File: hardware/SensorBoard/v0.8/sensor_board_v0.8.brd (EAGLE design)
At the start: 52.5 x 43 mm, 48 parts, among them IC1 BMP280, J3 USB-MICROB, U10 CCS811, U11 RFM69HW, U2 TSL2561, U3 ATMEGA328P-MU, U7 SHT31, U8 MCP1703/3.3V, U9 MCP1703CB, Y1 16MHZ

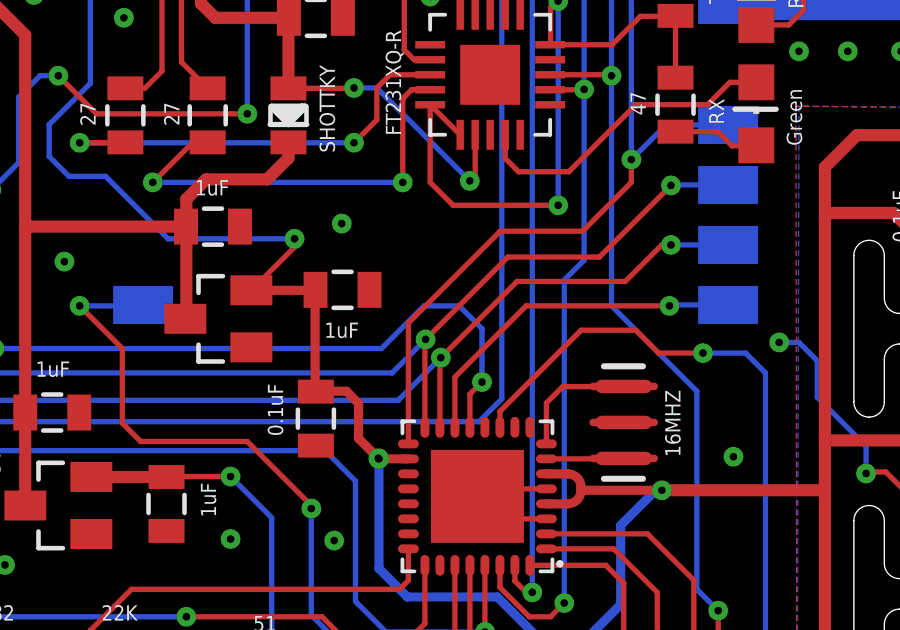
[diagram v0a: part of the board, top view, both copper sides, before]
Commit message: Adjusted distance between MISO and MOSI vias
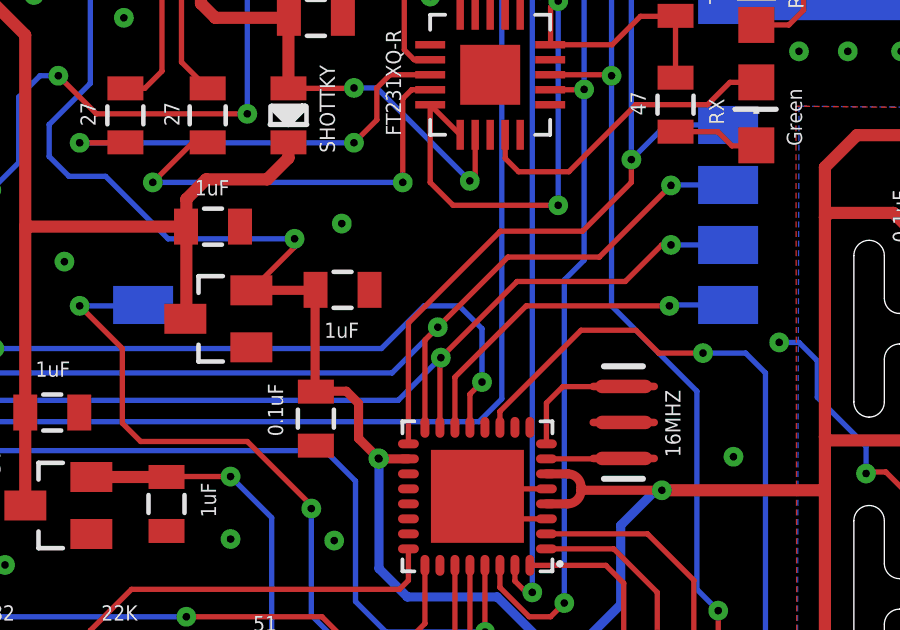
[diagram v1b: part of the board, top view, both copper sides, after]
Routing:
- net MISO: track 47.7 -> 48.3 mm
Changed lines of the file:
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@@
 <contactref element="U3" pad="16"/>
 <wire x1="13.5636" y1="30.5308" x2="27.3304" y2="30.5308" width="0.1778" layer="16"/>
-<wire x1="31.1912" y1="34.3916" x2="28.448" y2="31.6484" width="0.1778" layer="1"/>
-<via x="28.448" y="31.6484" extent="1-16" drill="0.254" diameter="0.127"/>
-<wire x1="28.448" y1="31.6484" x2="27.3304" y2="30.5308" width="0.1778" layer="16"/>
+<via x="28.8544" y="32.0548" extent="1-16" drill="0.254" diameter="0.127"/>
+<wire x1="28.8544" y1="32.0548" x2="27.3304" y2="30.5308" width="0.1778" layer="16"/>
 <wire x1="28.4252" y1="28.716" x2="28.4252" y2="31.6256" width="0.1778" layer="1"/>
-<wire x1="28.4252" y1="31.6256" x2="28.448" y2="31.6484" width="0.1778" layer="1"/>
+<wire x1="28.4252" y1="31.6256" x2="28.8544" y2="32.0548" width="0.1778" layer="1"/>
+<wire x1="31.1912" y1="34.3916" x2="28.8544" y2="32.0548" width="0.1778" layer="1"/>
 </signal>
 <signal name="SCK">
